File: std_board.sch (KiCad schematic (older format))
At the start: 192 parts, among them IC1 ESP32, IC2 ACS712, IC3 L78L05, IC4 AMS1117-V, J1 Jumper, J10 J_DHT11, J11 Jumper, J12 Jumper, J14 Jumper, J15 Jumper, J16 J_PRess, J17 Jumper, J18 Jumper, J19 Jumper, J2 Jumper, J20 Jumper, J21 Jumper, J22 Jumper, J23 Jumper, J24 Jumper, J25 Jumper, J26 Jumper, J3 Jumper, J31 Jumper, J32 Jumper, J33 Jumper, J34 Jumper, J35 Jumper, J36 Jumper, J37 Jumper, J38 Jumper, J39 Jumper, J4 Jumper, J40 Jumper, J41 Jumper, J42 Jumper, J43 Jumper, J44 Jumper, J45 Jumper, J5 Jumper, J7 Jumper, J8 Jumper, J9 Jumper, T1 TRIAC_Micro, T2 TRIAC_Micro, T3 TRIAC_Micro, T4 NPN_MMBT222A, T5 NPN_MMBT222A, T6 NPN_MMBT222A, T7 NPN_MMBT222A, T8 PNP_2N3906, T9 NPN_MMBT222A, U1 LNK306

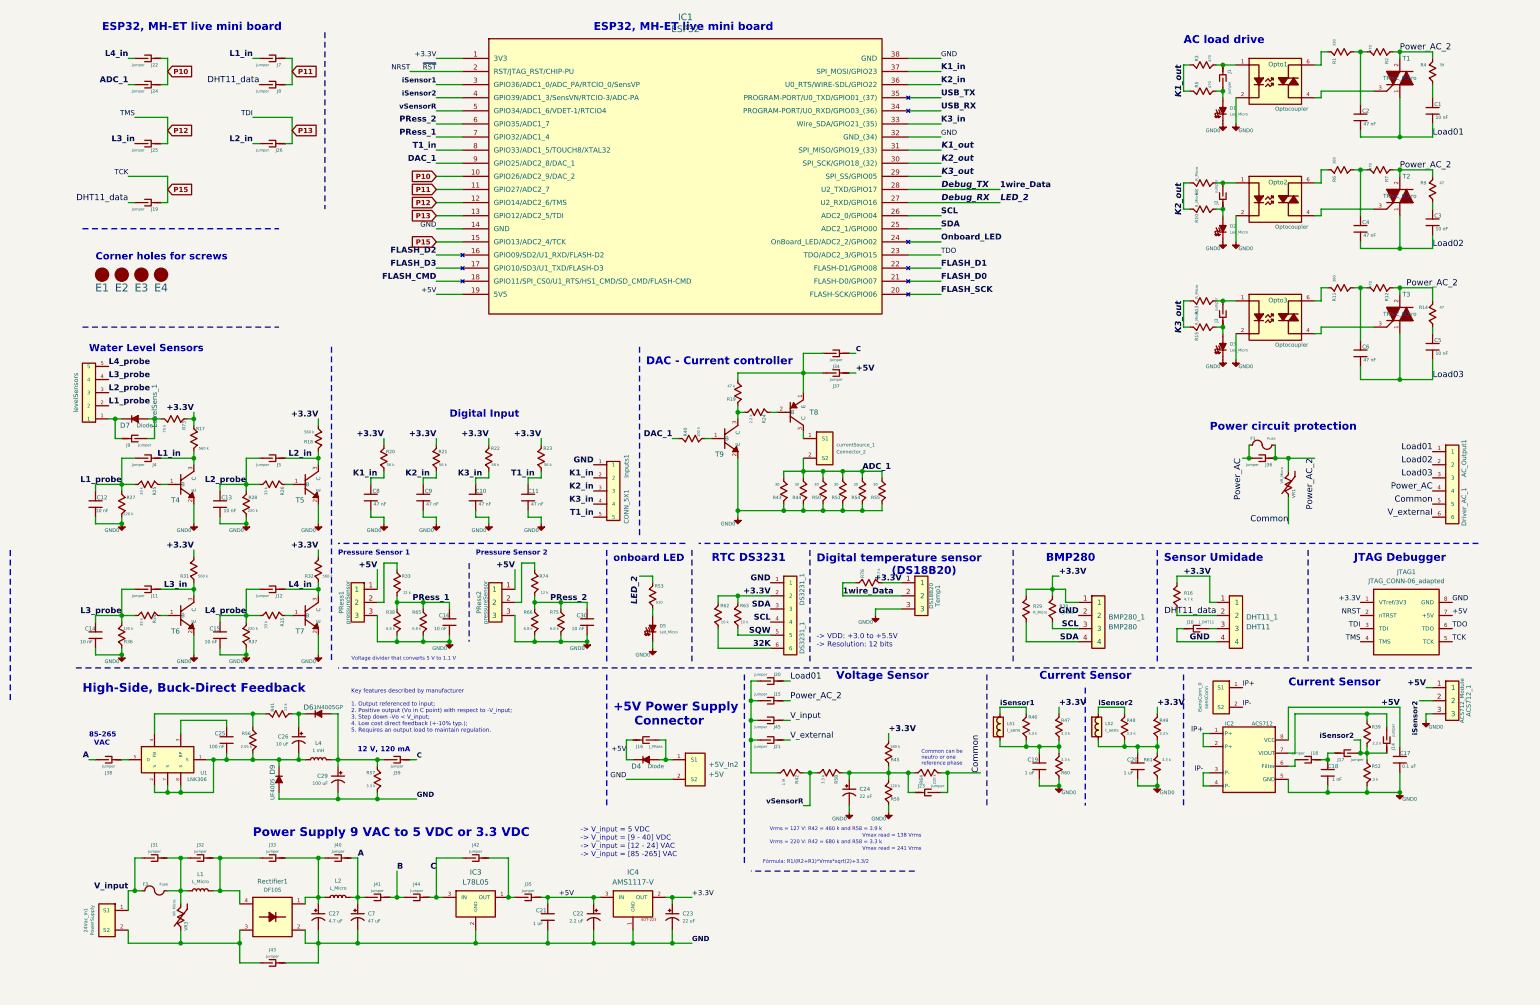
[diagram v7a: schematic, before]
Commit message: recalculated current sensor resistors and changed pins and jumps of levels and sensors
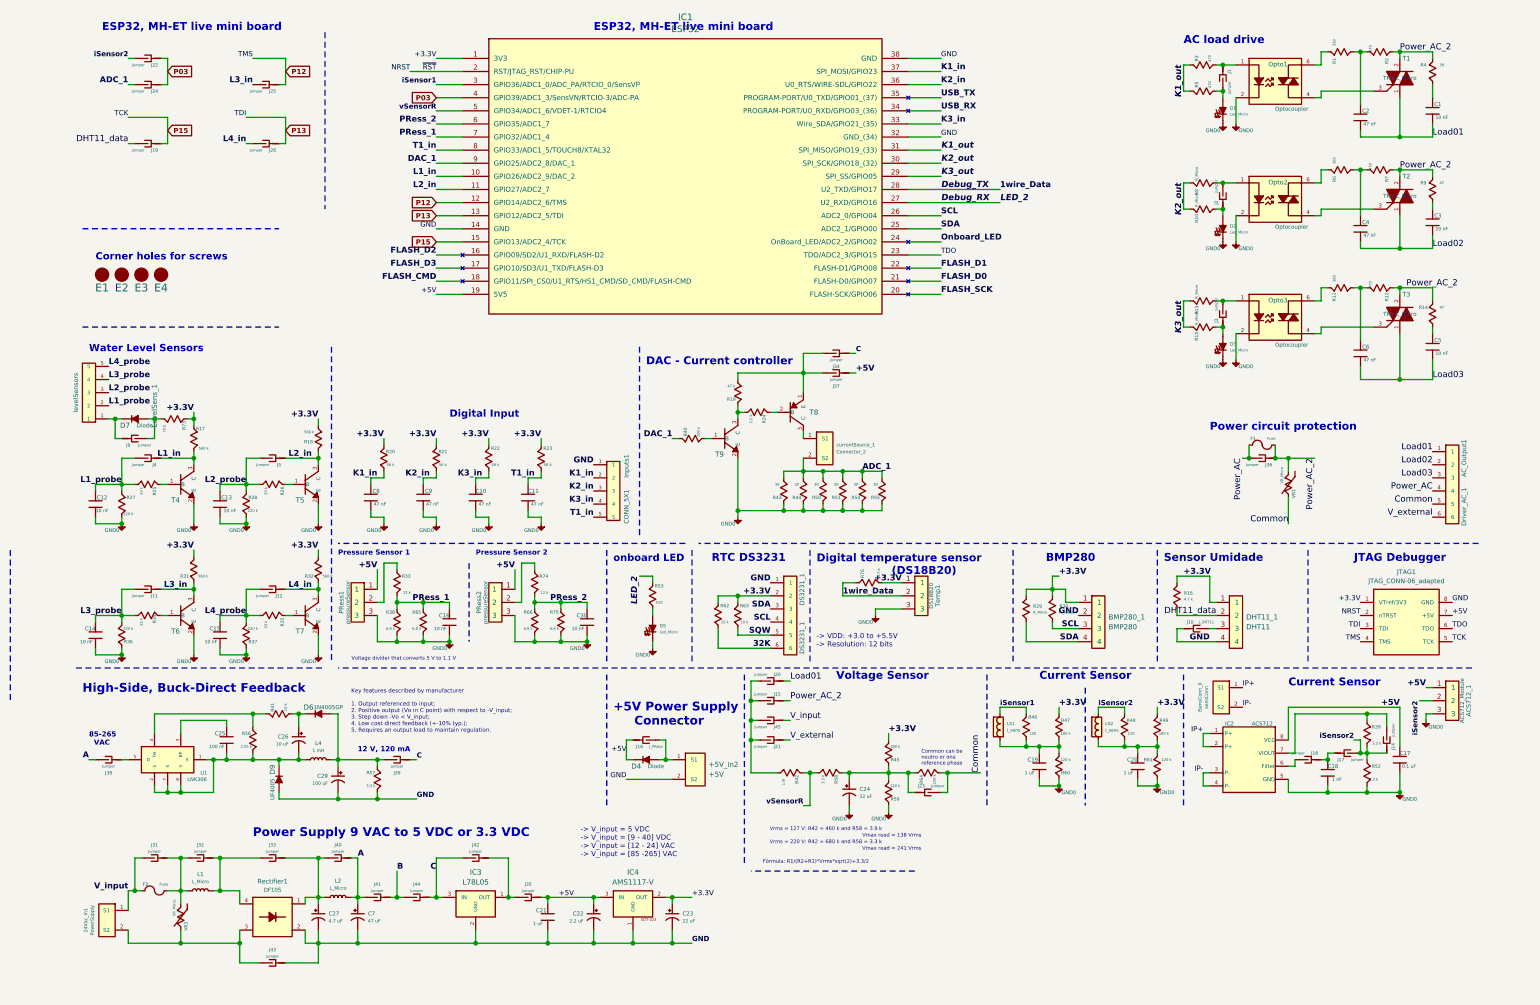
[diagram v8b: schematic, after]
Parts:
- removed J7, J8: Jumper, thmalmeida:J_0603, symbol std_board-rescue:Jumper-thmalmeida
- R46, R48: value 3.3 k -> 120
- R47, R49: value 3.3 k -> 180 k
- R60, R61: value 3.3 k -> 120 k
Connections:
- net P11 is gone; now on net L2_in: IC1.11 (GPIO27/ADC2_7)
- net L1_in: now also IC1.10 (GPIO26/ADC2_9/DAC_2)
- net L2_in: no longer J26.2 (B)
- net L4_in: now also J26.2 (B); no longer J22.2 (B)
- net iSensor2: now also J22.2 (B); no longer IC1.4 (GPIO39/ADC1_3/SensVN/RTCIO-3/ADC-PA)
- net P10 renamed P03
- net P03: now also IC1.4 (GPIO39/ADC1_3/SensVN/RTCIO-3/ADC-PA); no longer IC1.10 (GPIO26/ADC2_9/DAC_2)
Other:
- moved on the sheet: J19, J25, J26
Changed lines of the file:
@@
 P 7750 5900
 F 0 "R46" H 7800 5975 25  0000 C CNN
-F 1 "3.3 k" H 7800 5850 20  0000 C CNN
+F 1 "120" H 7800 5850 20  0000 C CNN
 F 2 "Resistor_SMD:R_0805_2012Metric" H 7580 5850 60  0001 C CNN
 F 3 "" H 7680 5950 60  0000 C CNN
@@
 P 8000 6200
 F 0 "R60" H 8050 6150 25  0000 C CNN
-F 1 "3.3 k" H 8050 6250 20  0000 C CNN
+F 1 "120 k" H 8050 6250 20  0000 C CNN
 F 2 "Resistor_SMD:R_0805_2012Metric" H 7830 6150 60  0001 C CNN
 F 3 "" H 7930 6250 60  0000 C CNN
@@
 P 8000 5900
 F 0 "R47" H 8050 5950 25  0000 C CNN
-F 1 "3.3 k" H 8050 5850 20  0000 C CNN
+F 1 "180 k" H 8050 5850 20  0000 C CNN
 F 2 "Resistor_SMD:R_0805_2012Metric" H 7830 5850 60  0001 C CNN
 F 3 "" H 7930 5950 60  0000 C CNN
@@
 P 8750 6200
 F 0 "R61" H 8680 6250 25  0000 C CNN
-F 1 "3.3 k" H 8820 6250 20  0000 C CNN
+F 1 "120 k" H 8820 6250 20  0000 C CNN
 F 2 "Resistor_SMD:R_0805_2012Metric" H 8580 6150 60  0001 C CNN
 F 3 "" H 8680 6250 60  0000 C CNN
@@
 P 8750 5900
 F 0 "R49" H 8800 5950 25  0000 C CNN
-F 1 "3.3 k" H 8800 5850 20  0000 C CNN
+F 1 "180 k" H 8800 5850 20  0000 C CNN
 F 2 "Resistor_SMD:R_0805_2012Metric" H 8580 5850 60  0001 C CNN
 F 3 "" H 8680 5950 60  0000 C CNN
@@
 Wire Wire Line
 	1550 7150 1600 7150
-Text Label 1850 800  2    45   ~ 9
+Text Label 3250 1700 2    45   ~ 9
 L1_in
 $Comp
-L std_board-rescue:Jumper-thmalmeida J7
-U 1 1 5F740ED2
-P 2000 800
-F 0 "J7" H 1950 850 25  0000 C CNN
-F 1 "Jumper" H 2075 850 20  0000 C CNN
-F 2 "thmalmeida:J_0603" H 2000 925 60  0001 C CNN
-F 3 "" H 2025 800 60  0000 C CNN
-	1    2000 800
-	-1   0    0    1
-$EndComp
-$Comp
-L std_board-rescue:Jumper-thmalmeida J8
-U 1 1 5F741B56
-P 2000 1000
-F 0 "J8" H 1950 1050 25  0000 C CNN
-F 1 "Jumper" H 2075 1050 20  0000 C CNN
-F 2 "thmalmeida:J_0603" H 2000 1125 60  0001 C CNN
-F 3 "" H 2025 1000 60  0000 C CNN
-	1    2000 1000
-	-1   0    0    1
-$EndComp
-Wire Wire Line
-	1850 800  1900 800
-Wire Wire Line
-	2100 800  2150 800
-Wire Wire Line
-	2150 800  2150 1000
-Wire Wire Line
-	2150 1000 2100 1000
-Text GLabel 2150 900  2    39   Input ~ 8
-P11
-$Comp
 L std_board-rescue:Jumper-thmalmeida J9
 U 1 1 5F85A4F6
@@
 L std_board-rescue:Jumper-thmalmeida J26
 U 1 1 605D8BF6
-P 2000 1450
-F 0 "J26" H 1950 1500 25  0000 C CNN
-F 1 "Jumper" H 2075 1500 20  0000 C CNN
-F 2 "thmalmeida:J_0603" H 2000 1575 60  0001 C CNN
-F 3 "" H 2025 1450 60  0000 C CNN
-	1    2000 1450
+P 1950 1450
+F 0 "J26" H 1900 1500 25  0000 C CNN
+F 1 "Jumper" H 2025 1500 20  0000 C CNN
+F 2 "thmalmeida:J_0603" H 1950 1575 60  0001 C CNN
+F 3 "" H 1975 1450 60  0000 C CNN
+	1    1950 1450
 	-1   0    0    1
 $EndComp
 Wire Wire Line
-	2150 1250 2150 1450
+	2100 1250 2100 1450
 Wire Wire Line
-	2150 1450 2100 1450
-Text GLabel 2150 1350 2    39   Input ~ 8
+	2100 1450 2050 1450
+Text GLabel 2100 1350 2    39   Input ~ 8
 P13
 $Comp
 L std_board-rescue:Jumper-thmalmeida J25
 U 1 1 605D8BFF
-P 1050 1450
-F 0 "J25" H 1000 1500 25  0000 C CNN
-F 1 "Jumper" H 1125 1500 20  0000 C CNN
-F 2 "thmalmeida:J_0603" H 1050 1575 60  0001 C CNN
-F 3 "" H 1075 1450 60  0000 C CNN
-	1    1050 1450
+P 1950 1000
+F 0 "J25" H 1900 1050 25  0000 C CNN
+F 1 "Jumper" H 2025 1050 20  0000 C CNN
+F 2 "thmalmeida:J_0603" H 1950 1125 60  0001 C CNN
+F 3 "" H 1975 1000 60  0000 C CNN
+	1    1950 1000
 	-1   0    0    1
 $EndComp
 Wire Wire Line
-	1200 1250 1200 1450
+	2100 800  2100 1000
 Wire Wire Line
-	1200 1450 1150 1450
-Text GLabel 1200 1350 2    39   Input ~ 8
+	2100 1000 2050 1000
+Text GLabel 2100 900  2    39   Input ~ 8
 P12
-Text Label 950  1250 2    39   ~ 0
+Text Label 1850 800  2    39   ~ 0
 TMS
-Text Label 1850 1250 2    39   ~ 0
+Text Label 1800 1250 2    39   ~ 0
 TDI
 Wire Wire Line
-	1850 1250 2150 1250
-Text Label 950  1450 2    45   ~ 9
+	1800 1250 2100 1250
+Text Label 1850 1000 2    45   ~ 9
 L3_in
-Text Label 1850 1450 2    45   ~ 9
+Text Label 3250 1800 2    45   ~ 9
 L2_in
 $Comp
@@
 Wire Wire Line
 	1200 1000 1150 1000
-Text GLabel 1200 900  2    39   Input ~ 8
-P10
 Text Label 3250 1600 2    45   ~ 9
 DAC_1
-Text GLabel 3250 1700 0    39   Input ~ 8
-P10
-Text GLabel 3250 1800 0    39   Input ~ 8
-P11
 Text GLabel 3250 1900 0    39   Input ~ 8
 P12
@@
 Text Label 3250 1000 2    39   ~ 8
 iSensor1
-Text Label 3250 1100 2    39   ~ 8
+Text Label 900  800  2    39   ~ 8
 iSensor2
 Wire Wire Line
@@
 Text Label 10300 4950 2    39   ~ 0
 +3.3V
-Text Label 900  800  2    45   ~ 9
+Text Label 1800 1450 2    45   ~ 9
 L4_in
 Wire Wire Line
-	950  1250 1200 1250
+	1850 800  2100 800
 $Comp
 L std_board-rescue:R_Micro-thmalmeida R45
@@
 $EndComp
 Wire Wire Line
-	1900 1450 1850 1450
+	1850 1450 1800 1450
 Wire Wire Line
 	3250 2000 3450 2000
@@
 P 8500 5900
 F 0 "R48" H 8550 5950 25  0000 C CNN
-F 1 "3.3 k" H 8550 5850 20  0000 C CNN
+F 1 "120" H 8550 5850 20  0000 C CNN
 F 2 "Resistor_SMD:R_0805_2012Metric" H 8330 5850 60  0001 C CNN
 F 3 "" H 8430 5950 60  0000 C CNN
@@
 Wire Wire Line
 	4800 4750 4900 4750
-Text Label 1900 1000 2    47   ~ 0
-DHT11_data
 Text Label 7550 1900 0    47   Italic 9
 LED_2
@@
 Wire Wire Line
 	950  1000 900  1000
-Text GLabel 1200 1800 2    39   Input ~ 8
+Text GLabel 1200 1350 2    39   Input ~ 8
 P15
 $Comp
 L std_board-rescue:Jumper-thmalmeida J19
 U 1 1 603F856A
-P 1050 1900
-F 0 "J19" H 1000 1950 25  0000 C CNN
-F 1 "Jumper" H 1125 1950 20  0000 C CNN
-F 2 "thmalmeida:J_0603" H 1050 2025 60  0001 C CNN
-F 3 "" H 1075 1900 60  0000 C CNN
-	1    1050 1900
+P 1050 1450
+F 0 "J19" H 1000 1500 25  0000 C CNN
+F 1 "Jumper" H 1125 1500 20  0000 C CNN
+F 2 "thmalmeida:J_0603" H 1050 1575 60  0001 C CNN
+F 3 "" H 1075 1450 60  0000 C CNN
+	1    1050 1450
 	-1   0    0    1
 $EndComp
-Text Label 900  1700 2    39   ~ 0
+Text Label 900  1250 2    39   ~ 0
 TCK
 Wire Wire Line
-	900  1700 1200 1700
+	900  1250 1200 1250
 Wire Wire Line
-	1200 1700 1200 1900
+	1200 1250 1200 1450
 Wire Wire Line
-	1200 1900 1150 1900
+	1200 1450 1150 1450
 Wire Wire Line
-	950  1900 900  1900
-Text Label 900  1900 2    47   ~ 0
+	950  1450 900  1450
+Text Label 900  1450 2    47   ~ 0
 DHT11_data
 Text Notes 4850 3150 0    60   ~ 12
@@
 Wire Wire Line
 	4200 4950 4400 4950
+Text GLabel 1200 900  2    39   Input ~ 8
+P03
+Text GLabel 3250 1100 0    39   Input ~ 8
+P03
 $EndSCHEMATC
